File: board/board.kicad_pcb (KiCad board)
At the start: 2 copper layers, 100 x 64 mm, 10 parts, among them J1 RJ12, J10 PLAN, J2 JST XH, J3 JST XH, J4 RJ12, J5 Barrel_Jack, J6 Seriale, J7 MPX, J8 Conn_02x10_Counter_Clockwise_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, J9 Seriale

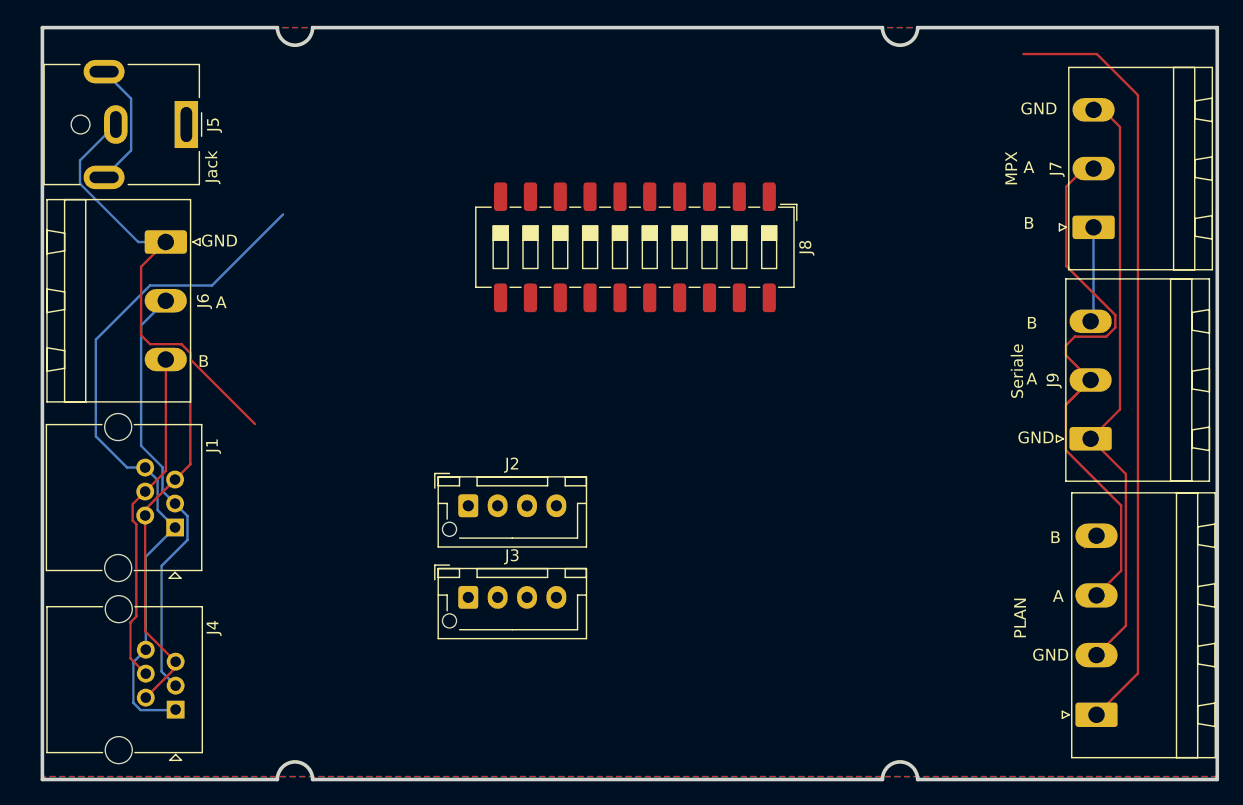
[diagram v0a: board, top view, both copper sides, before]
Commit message: [ADD] Add new sockets
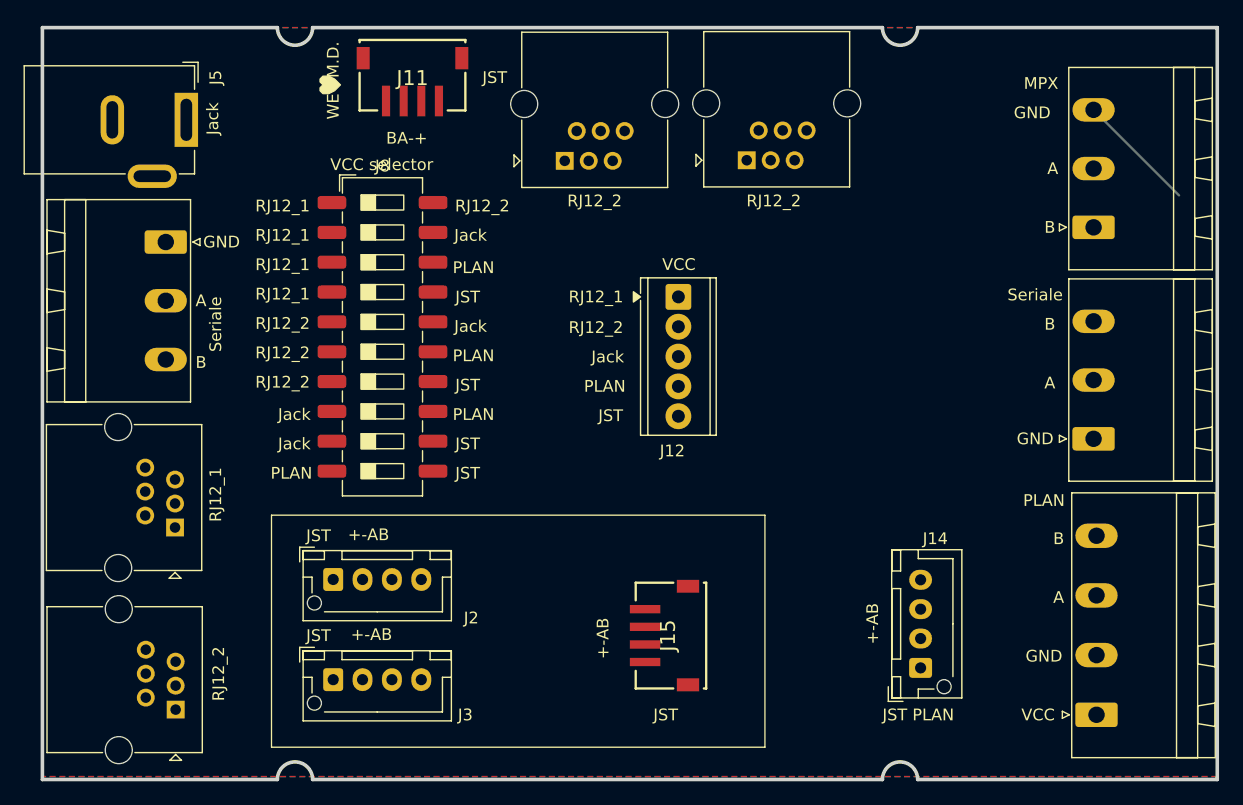
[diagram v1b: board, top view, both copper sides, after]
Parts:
- added J11: REMOTE_DISPLAY, board:648104131822, F.Cu at (123.0, 54.5)
- added J12: Conn_01x05_Socket, TerminalBlock_Phoenix:TerminalBlock_Phoenix_MPT-0,5-5-2.54_1x05_P2.54mm_Horizontal, F.Cu at (145.6, 73.4)
- added J13: RJ12, Connector_RJ:RJ25_Wayconn_MJEA-660X1_Horizontal, F.Cu at (136.0, 61.8)
- added J14: JST PLAN, Connector_JST:JST_XH_B4B-XH-AM_1x04_P2.50mm_Vertical, F.Cu at (166.2, 105.0)
- added J15: REMOTE_DISPLAY, board:648104131822, F.Cu at (145.0, 102.2)
- added J16: RJ12, Connector_RJ:RJ25_Wayconn_MJEA-660X1_Horizontal, F.Cu at (151.4, 61.8)
- J5: footprint Connector_BarrelJack:BarrelJack_CUI_PJ-063AH_Horizontal -> Connector_BarrelJack:BarrelJack_GCT_DCJ200-10-A_Horizontal
- moved J8 22.8 mm to (120.4, 76.8), turned to 0 degrees
- moved J3 13.5 mm to (116.2, 106.0)
- moved J2 13.1 mm to (116.2, 97.5)
- moved J5 0.40 mm to (103.8, 58.4)
- moved J9 0.25 mm to (181.0, 85.5)
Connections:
- J1 pad 1: /vcc_RJ12 -> /vcc_RJ12_1
- J4 pad 1: /vcc_RJ12 -> /vcc_RJ12_2
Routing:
- net /gnd: track 121.2 -> 10.3 mm
- net /A: track 86.9 -> 0.00 mm
- net /vcc_PLAN: track 65.4 -> 0.00 mm
- net /vcc_RJ12: track 60.3 -> 0.00 mm
- net /B: track 38.3 -> 0.00 mm
- net (no net): track 10.9 -> 0.00 mm
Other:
- board text added: "+-AB"
- board text added: "BA-+"
- board text added: "JST"
- board text added: "PLAN"
- board text added: "RJ12_1"
- board text added: "RJ12_2"
- board text added: "Seriale"
- board text added: "VCC"
- board text added: "VCC selector"
- board text added: "WE M.D."

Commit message: [UPD] Update image
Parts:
- moved J10 0.22 mm to (181.0, 109.0)
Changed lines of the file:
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@@
 	(footprint "Connector_Phoenix_MSTB:PhoenixContact_MSTBA_2,5_4-G-5,08_1x04_P5.08mm_Horizontal"
 		(layer "F.Cu")
-		(at 181.2225 108.99 90)
+		(at 181 108.99 90)
 		(descr "Generic Phoenix Contact connector footprint for: MSTBA_2,5/4-G-5,08; number of pins: 04; pin pitch: 5.08mm; Angled || order number: 1757268 12A || order number: 1923885 16A (HC)")
 		(tags "phoenix_contact connector MSTBA_01x04_G_5.08mm")
@@
 		(tags "SMD DIP Switch SPST Slide 8.61mm 338mil SMD LowProfile")
 		(property "Reference" "J8"
-			(at 0 -14.54 0)
+			(at 4.805 14.43 0)
 			(layer "F.SilkS")
 			(effects
@@
 		)
 		(property "Value" "MPX"
-			(at 12.25 -4.4725 0)
+			(at 13.25 -4.2225 0)
 			(layer "F.SilkS")
 			(effects
@@
 		)
 		(property "Value" "Seriale"
-			(at 12.25 -4.9725 180)
+			(at 13.25 -5.2225 180)
 			(layer "F.SilkS")
 			(effects
@@
 	)
 	(gr_text "GND\n"
-		(at 175.75 57.75 0)
+		(at 176.5 57.75 0)
 		(layer "F.SilkS")
 		(effects
@@
 	)
 	(gr_text "PLAN\n"
-		(at 176.75 90.75 0)
+		(at 176.25 90.75 0)
 		(layer "F.SilkS")
 		(effects
@@
 	)
 	(gr_text "B"
-		(at 178 94 0)
+		(at 177.5 94 0)
 		(layer "F.SilkS")
 		(effects
@@
 	)
 	(gr_text "GND"
-		(at 176.75 104 0)
+		(at 176.5 104 0)
 		(layer "F.SilkS")
 		(effects
@@
 	)
 	(gr_text "A"
-		(at 178 99 0)
+		(at 177.5 99 0)
 		(layer "F.SilkS")
 		(effects

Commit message: [UPD] Final version for JLCPCB
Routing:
- net /gnd: track 10.3 -> 288.0 mm
- net /A: track 0.00 -> 276.1 mm
- net /B: track 0.00 -> 223.8 mm
- net /vcc_RJ12_2: track 0.00 -> 122.1 mm
- net /vcc_JST: track 0.00 -> 121.8 mm, vias 0 -> 6
- net /vcc_PLAN: track 0.00 -> 103.2 mm
- net /vcc_RJ12_1: track 0.00 -> 99.4 mm, vias 0 -> 4
- net /vcc_jack: track 0.00 -> 74.7 mm, vias 0 -> 2
